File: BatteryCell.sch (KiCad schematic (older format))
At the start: 8 parts

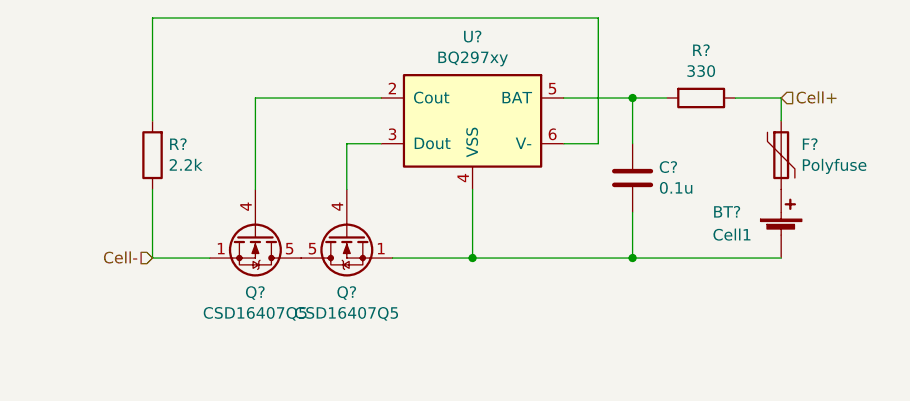
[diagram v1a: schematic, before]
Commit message: Added 5MOhm resistor across gatesource of power mosfet in battery cell protection schematic
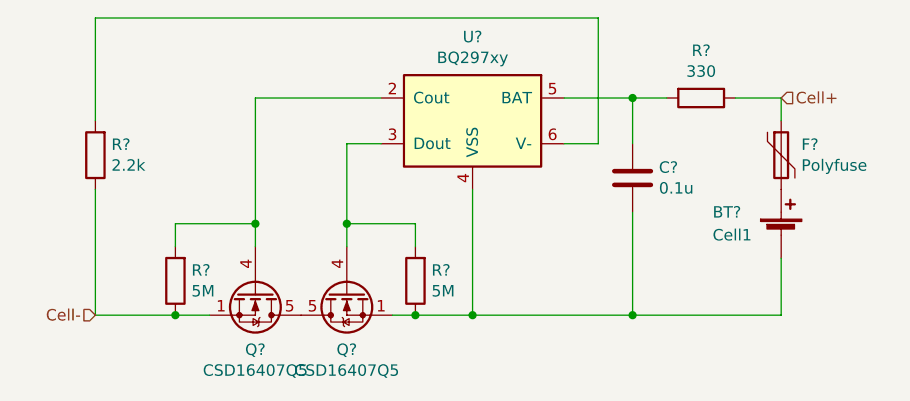
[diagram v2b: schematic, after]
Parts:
- added R? (x2): 5M, symbol Device:R
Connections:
- net Cell-: now also R?.1
- net at BT?.2 (-), C?.2, Q?.1 (S)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: now also R?.1
- net at Q?.4 (G), U?.2 (Cout): now also R?.2
- net at Q?.4 (G), U?.3 (Dout): now also R?.2
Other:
- moved on the sheet: Q?, R?
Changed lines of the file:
@@
 L Transistor_FET:CSD16407Q5 Q?
 U 1 1 5D087B4E
-P 4750 4100
+P 4750 4350
 AR Path="/5D087B4E" Ref="Q?"  Part="1"
 AR Path="/5D07F3FC/5D087B4E" Ref="Q?"  Part="1"
@@
 AR Path="/5D0B1FBC/5D087B4E" Ref="Q?"  Part="1"
 AR Path="/5D0BC9BA/5D087B4E" Ref="Q?"  Part="1"
-F 0 "Q?" V 5001 4100 50  0000 C CNN
-F 1 "CSD16407Q5" V 5092 4100 50  0000 C CNN
-F 2 "Package_TO_SOT_SMD:TDSON-8-1" H 4950 4025 50  0001 L CIN
-F 3 "http://www.ti.com/lit/gpn/csd16407q5" V 4750 4100 50  0001 L CNN
-	1    4750 4100
+F 0 "Q?" V 5001 4350 50  0000 C CNN
+F 1 "CSD16407Q5" V 5092 4350 50  0000 C CNN
+F 2 "Package_TO_SOT_SMD:TDSON-8-1" H 4950 4275 50  0001 L CIN
+F 3 "http://www.ti.com/lit/gpn/csd16407q5" V 4750 4350 50  0001 L CNN
+	1    4750 4350
 	0    1    1    0
 $EndComp
@@
 L Transistor_FET:CSD16407Q5 Q?
 U 1 1 5D087B54
-P 5150 4100
+P 5150 4350
 AR Path="/5D087B54" Ref="Q?"  Part="1"
 AR Path="/5D07F3FC/5D087B54" Ref="Q?"  Part="1"
@@
 AR Path="/5D0B1FBC/5D087B54" Ref="Q?"  Part="1"
 AR Path="/5D0BC9BA/5D087B54" Ref="Q?"  Part="1"
-F 0 "Q?" V 5401 4100 50  0000 C CNN
-F 1 "CSD16407Q5" V 5492 4100 50  0000 C CNN
-F 2 "Package_TO_SOT_SMD:TDSON-8-1" H 5350 4025 50  0001 L CIN
-F 3 "http://www.ti.com/lit/gpn/csd16407q5" V 5150 4100 50  0001 L CNN
-	1    5150 4100
+F 0 "Q?" V 5401 4350 50  0000 C CNN
+F 1 "CSD16407Q5" V 5492 4350 50  0000 C CNN
+F 2 "Package_TO_SOT_SMD:TDSON-8-1" H 5350 4275 50  0001 L CIN
+F 3 "http://www.ti.com/lit/gpn/csd16407q5" V 5150 4350 50  0001 L CNN
+	1    5150 4350
 	0    -1   1    0
 $EndComp
@@
 	5300 3700 5150 3700
 Wire Wire Line
-	5150 3700 5150 3900
-Wire Wire Line
 	5300 3500 4750 3500
 Wire Wire Line
-	4750 3500 4750 3900
-Wire Wire Line
-	5700 3900 5700 4200
-Wire Wire Line
-	5700 4200 5350 4200
+	5700 4450 5450 4450
 $Comp
 L Device:R R?
@@
 	6400 3500 6550 3500
 Wire Wire Line
-	5700 4200 6400 4200
-Connection ~ 5700 4200
+	5700 4450 6400 4450
+Connection ~ 5700 4450
+Connection ~ 6400 4450
 Wire Wire Line
-	6400 4200 6400 4000
-Connection ~ 6400 4200
-Wire Wire Line
-	6400 4200 7050 4200
+	6400 4450 7050 4450
 Wire Wire Line
 	6100 3700 6250 3700
@@
 	6250 3700 6250 3150
 Wire Wire Line
-	6250 3150 4300 3150
-Wire Wire Line
-	4300 3150 4300 3600
+	4050 3150 4050 3600
 $Comp
 L Device:R R?
 U 1 1 5D087B7B
-P 4300 3750
+P 4050 3750
 AR Path="/5D087B7B" Ref="R?"  Part="1"
 AR Path="/5D07F3FC/5D087B7B" Ref="R?"  Part="1"
@@
 AR Path="/5D0B1FBC/5D087B7B" Ref="R?"  Part="1"
 AR Path="/5D0BC9BA/5D087B7B" Ref="R?"  Part="1"
-F 0 "R?" H 4230 3704 50  0000 R CNN
-F 1 "2.2k" H 4230 3795 50  0000 R CNN
-F 2 "" V 4230 3750 50  0001 C CNN
-F 3 "~" H 4300 3750 50  0001 C CNN
-	1    4300 3750
+F 0 "R?" H 3980 3704 50  0000 R CNN
+F 1 "2.2k" H 3980 3795 50  0000 R CNN
+F 2 "" V 3980 3750 50  0001 C CNN
+F 3 "~" H 4050 3750 50  0001 C CNN
+	1    4050 3750
+	-1   0    0    1
+$EndComp
+Text HLabel 7050 3500 2    50   Input ~ 0
+Cell+
+Text HLabel 4050 4450 0    50   Input ~ 0
+Cell-
+$Comp
+L Device:R R?
+U 1 1 5CF617A0
+P 5450 4300
+AR Path="/5CF617A0" Ref="R?"  Part="1"
+AR Path="/5D07F3FC/5CF617A0" Ref="R?"  Part="1"
+AR Path="/5D0A75A0/5CF617A0" Ref="R?"  Part="1"
+AR Path="/5D0B1FBC/5CF617A0" Ref="R?"  Part="1"
+AR Path="/5D0BC9BA/5CF617A0" Ref="R?"  Part="1"
+F 0 "R?" H 5380 4254 50  0000 R CNN
+F 1 "5M" H 5380 4345 50  0000 R CNN
+F 2 "" V 5380 4300 50  0001 C CNN
+F 3 "~" H 5450 4300 50  0001 C CNN
+	1    5450 4300
 	-1   0    0    1
 $EndComp
 Wire Wire Line
-	4300 3900 4300 4200
+	7050 4200 7050 4450
 Wire Wire Line
-	4300 4200 4550 4200
-Text HLabel 7050 3500 2    50   Input ~ 0
-Cell+
-Text HLabel 4300 4200 0    50   Input ~ 0
-Cell-
+	6400 4000 6400 4450
+Wire Wire Line
+	5700 3900 5700 4450
+Wire Wire Line
+	5150 3700 5150 4050
+Wire Wire Line
+	4750 3500 4750 4050
+Wire Wire Line
+	4050 3900 4050 4450
+$Comp
+L Device:R R?
+U 1 1 5CF6AE03
+P 4400 4300
+AR Path="/5CF6AE03" Ref="R?"  Part="1"
+AR Path="/5D07F3FC/5CF6AE03" Ref="R?"  Part="1"
+AR Path="/5D0A75A0/5CF6AE03" Ref="R?"  Part="1"
+AR Path="/5D0B1FBC/5CF6AE03" Ref="R?"  Part="1"
+AR Path="/5D0BC9BA/5CF6AE03" Ref="R?"  Part="1"
+F 0 "R?" H 4330 4254 50  0000 R CNN
+F 1 "5M" H 4330 4345 50  0000 R CNN
+F 2 "" V 4330 4300 50  0001 C CNN
+F 3 "~" H 4400 4300 50  0001 C CNN
+	1    4400 4300
+	-1   0    0    1
+$EndComp
+Wire Wire Line
+	4050 3150 6250 3150
+Connection ~ 5450 4450
+Wire Wire Line
+	5450 4450 5350 4450
+Connection ~ 4400 4450
+Wire Wire Line
+	4400 4450 4550 4450
+Wire Wire Line
+	4050 4450 4400 4450
+Wire Wire Line
+	4400 4150 4400 4050
+Wire Wire Line
+	4400 4050 4750 4050
+Connection ~ 4750 4050
+Wire Wire Line
+	4750 4050 4750 4150
+Wire Wire Line
+	5450 4150 5450 4050
+Wire Wire Line
+	5450 4050 5150 4050
+Connection ~ 5150 4050
+Wire Wire Line
+	5150 4050 5150 4150
 $EndSCHEMATC
